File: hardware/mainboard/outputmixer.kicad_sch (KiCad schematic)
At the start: 15 parts, among them J10 MIX, J9 EXT, U12 TL074, U8 TL074

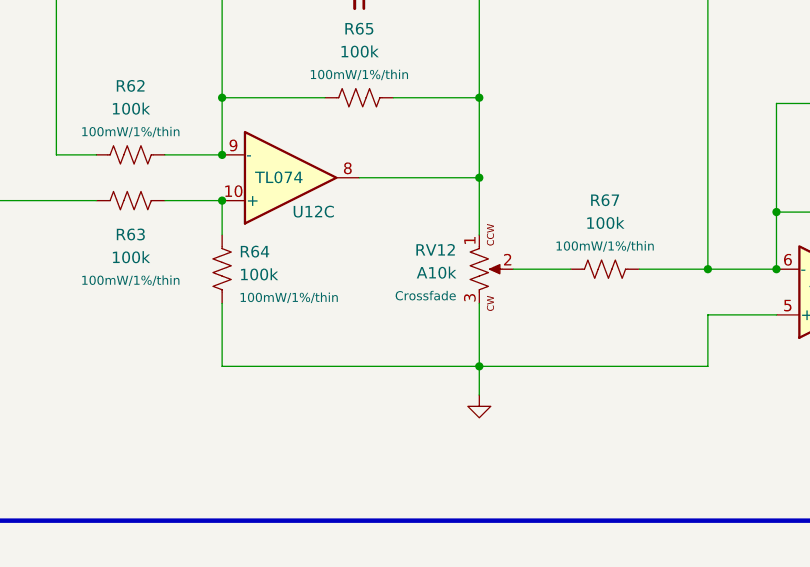
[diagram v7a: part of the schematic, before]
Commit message: hardware: update some labels, fix some fields, re-do fancytext
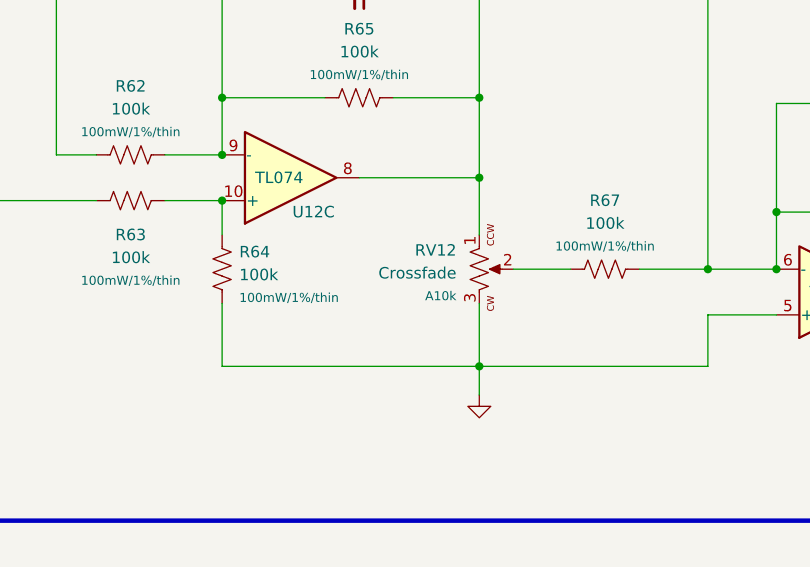
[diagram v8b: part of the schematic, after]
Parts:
- RV12: value A10k -> Crossfade; Rating Crossfade -> A10k
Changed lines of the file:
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@@
       (effects (font (size 1.27 1.27)) (justify left))
     )
-    (property "Value" "A10k" (id 1) (at 97.79 77.9144 90)
+    (property "Value" "Crossfade" (id 1) (at 97.79 77.9144 90)
       (effects (font (size 1.27 1.27)) (justify left))
     )
@@
       (effects (font (size 1.27 1.27)) hide)
     )
-    (property "Rating" "Crossfade" (id 7) (at 97.79 80.4545 90)
+    (property "Rating" "A10k" (id 7) (at 97.79 80.4545 90)
       (effects (font (size 1 1)) (justify left))
     )
